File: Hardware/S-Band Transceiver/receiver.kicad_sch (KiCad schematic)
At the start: 61 parts, among them J1 SMA, J6 SMA, J8 SMA, U1 LT1819, U15 TSS-53LNB3+, U17 SKY16603-632LF, U18 LT1819, U20 DCW-22-332+, U21 ADL5906

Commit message: Updates to schematic
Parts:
- added R59: 0, symbol Device:R_Small_US
- added U4: SN74LVC1G125DCK, Package_TO_SOT_SMD:SOT-23-5, symbol 74xGxx:SN74LVC1G125DCK
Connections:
- net GND: now also R59.1, U4.3 (GND)
- net IQ_MIXER_EN: now also R59.2
- net RX_AMP_EN: now also U4.2; no longer R16.2, U15.11 (EN)
- net +3V3_RX_AMP renamed +3.3VA
- net +3.3VA: now also U4.5 (VCC)
- new net: R16.2, U15.11 (EN), U4.4

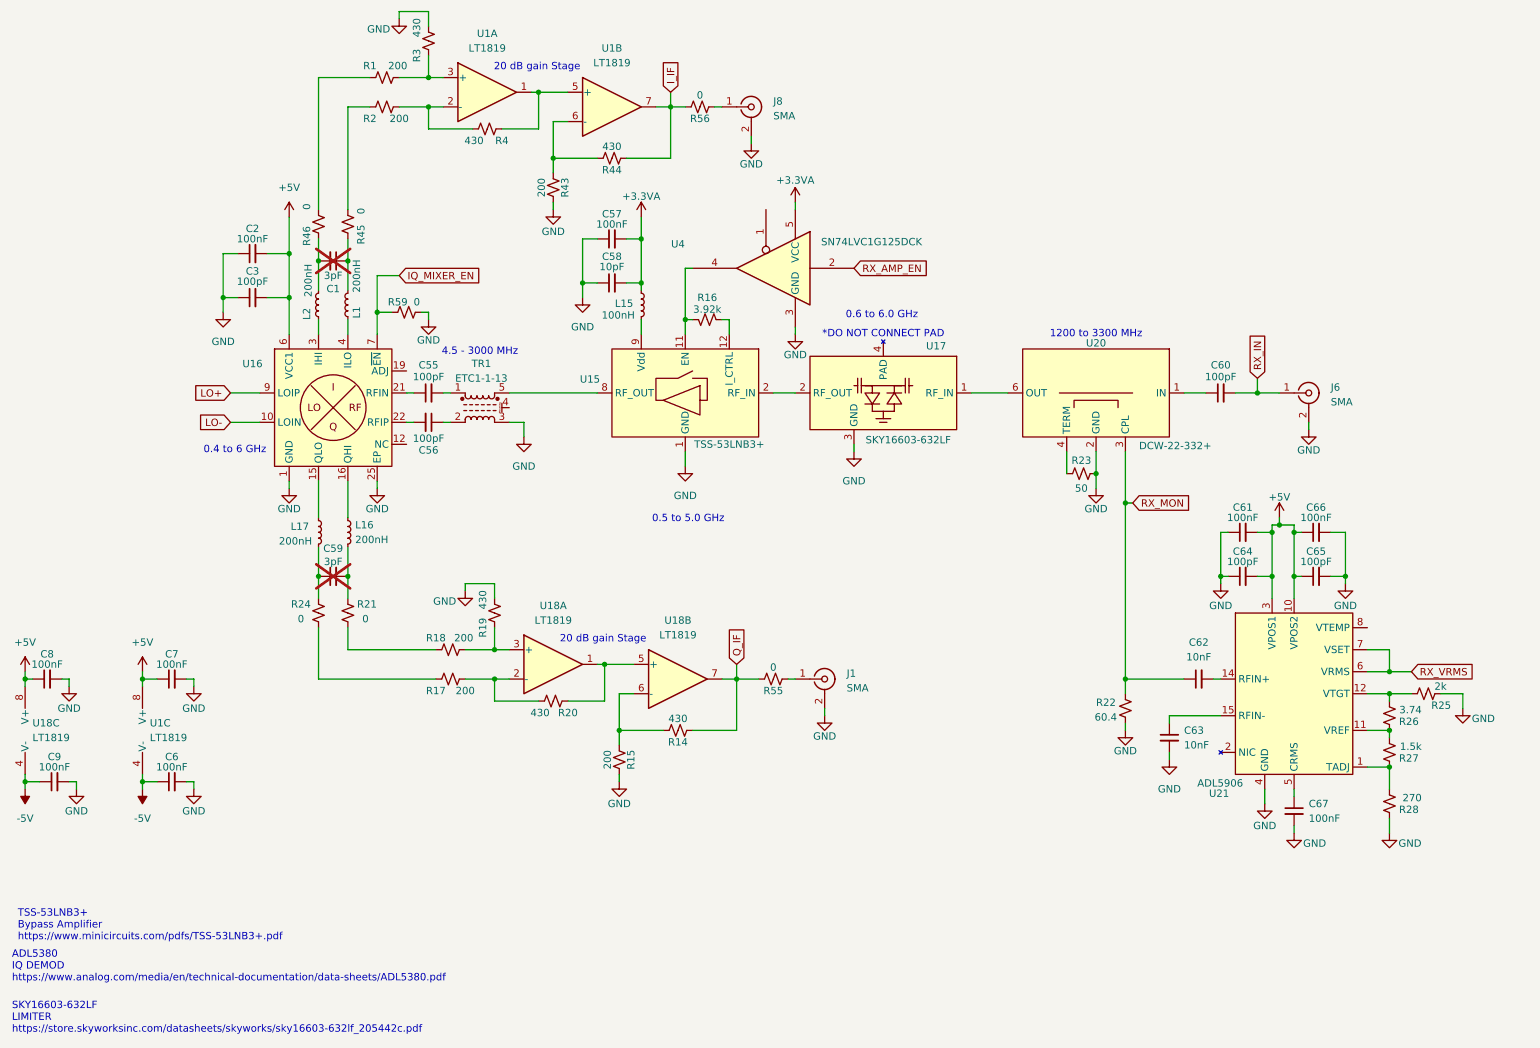
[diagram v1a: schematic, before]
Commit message: Updates to Schematic
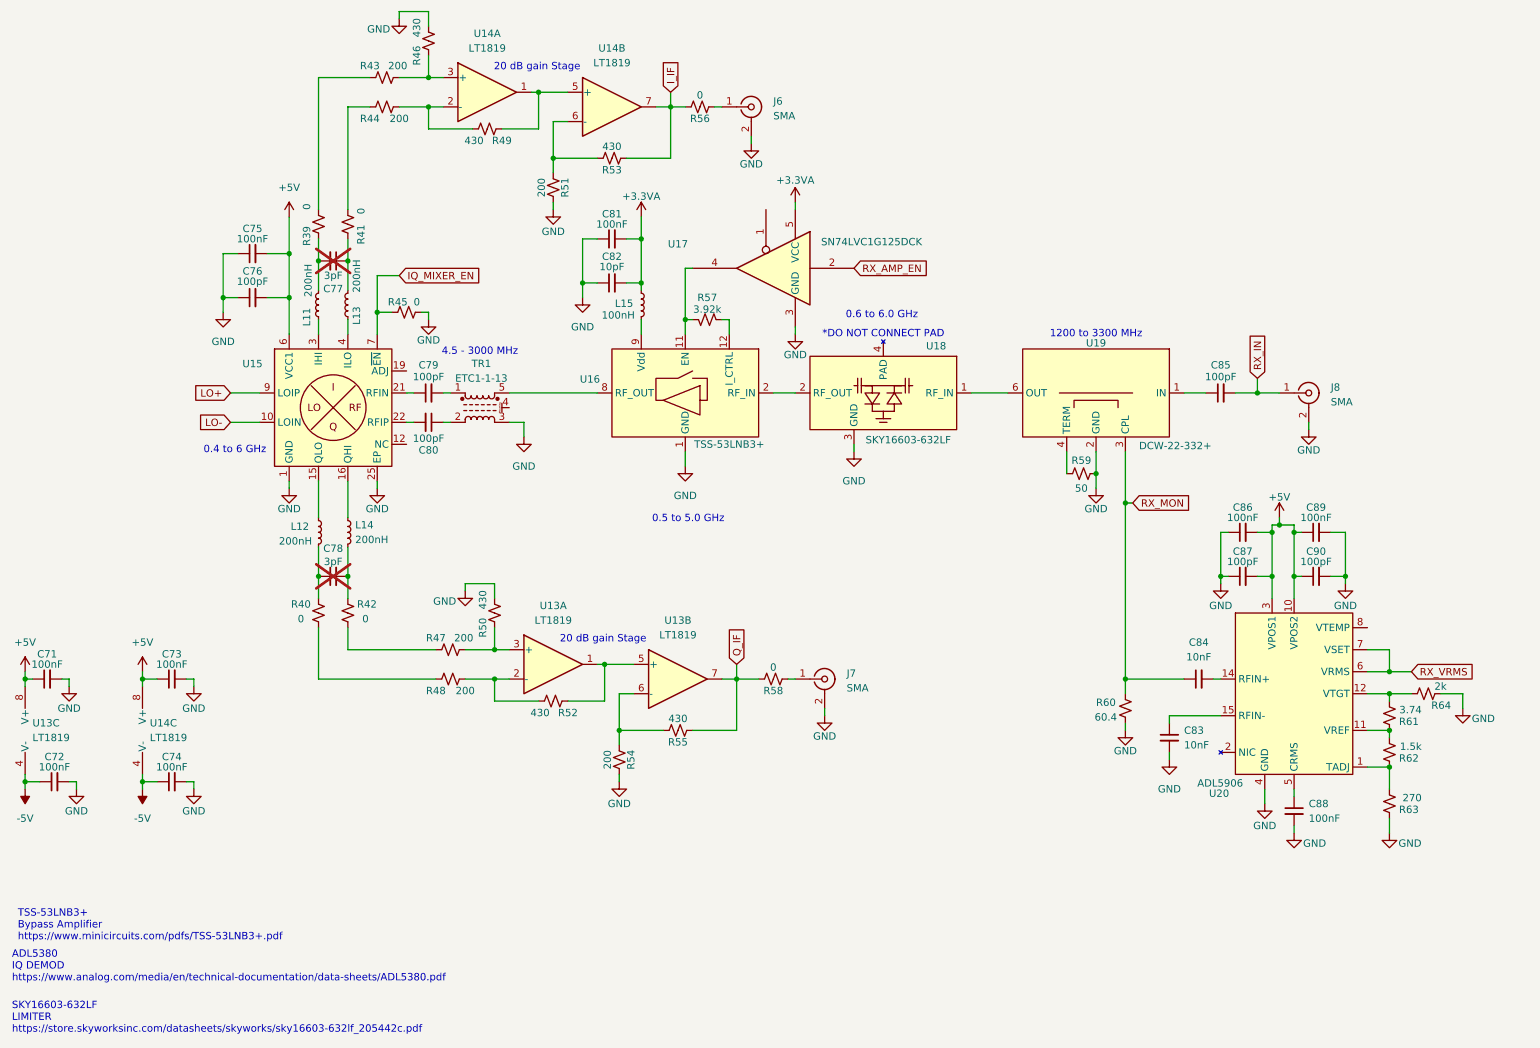
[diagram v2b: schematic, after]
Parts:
- renumbered C8 to C71, C9 to C72, C7 to C73, C6 to C74, C2 to C75, C3 to C76, C1 to C77, C59 to C78, C55 to C79, C56 to C80, C57 to C81, C58 to C82, C63 to C83, C62 to C84, C60 to C85, C61 to C86, C64 to C87, C67 to C88, C66 to C89, C65 to C90, J8 to J6, J1 to J7, J6 to J8, L2 to L11, L17 to L12, L1 to L13, L16 to L14, R46 to R39, R24 to R40, R45 to R41, R21 to R42, R1 to R43, R2 to R44, R59 to R45, R3 to R46, R18 to R47, R17 to R48, R4 to R49, R19 to R50, R43 to R51, R20 to R52, R44 to R53, R15 to R54, R14 to R55, R16 to R57, R55 to R58, R23 to R59, R22 to R60, R26 to R61, R27 to R62, R28 to R63, R25 to R64, U18 to U13, U1 to U14, U16 to U15, U15 to U16, U4 to U17, U17 to U18, U20 to U19, U21 to U20

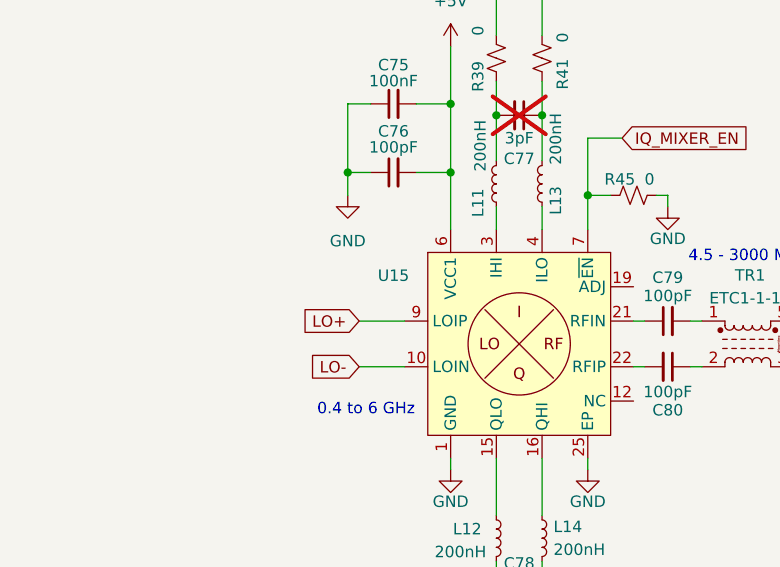
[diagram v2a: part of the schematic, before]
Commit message: Finished assigning footprints and starting board layout
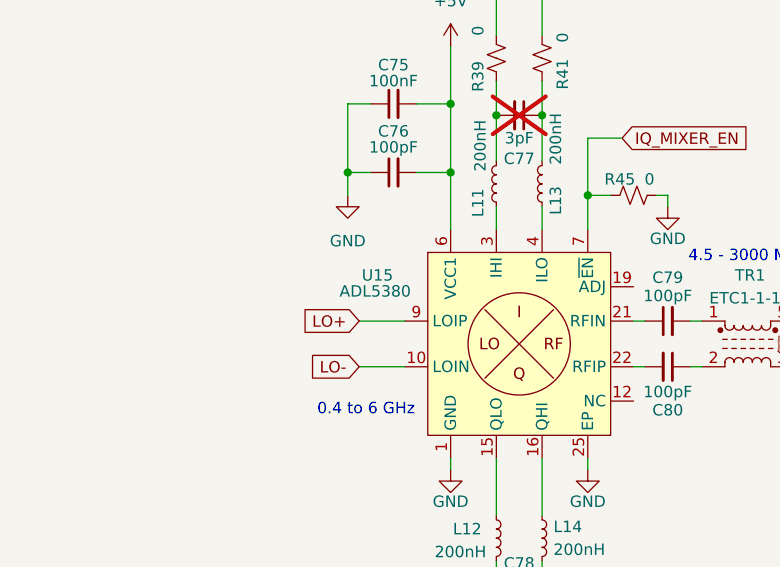
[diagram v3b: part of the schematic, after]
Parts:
- C71, C72, C73, C74, C75, C76, C77, C78, C79, C80, C81, C82, C83, C84, C85, C86, C87, C88, C89, C90: footprint (none) -> Capacitor_SMD:C_0402_1005Metric
- J6, J7, J8: footprint (none) -> Connector_Coaxial:SMA_Samtec_SMA-J-P-X-ST-EM1_EdgeMount
- L11, L12, L13, L14, L15: footprint (none) -> Inductor_SMD:L_0402_1005Metric
- R39, R40, R41, R42, R43, R44, R45, R46, R47, R48, R49, R50, R51, R52, R53, R54, R55, R56, R57, R58, R59, R60, R61, R62, R63, R64: footprint (none) -> Resistor_SMD:R_0603_1608Metric
- U15: value ~ -> ADL5380
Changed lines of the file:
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@@
 			)
 		)
-		(property "Footprint" ""
+		(property "Footprint" "Resistor_SMD:R_0603_1608Metric"
 			(at 149.86 132.08 0)
 			(effects
@@
 			)
 		)
-		(property "Footprint" ""
+		(property "Footprint" "Resistor_SMD:R_0603_1608Metric"
 			(at 133.35 140.97 0)
 			(effects
@@
 			)
 		)
-		(property "Footprint" ""
+		(property "Footprint" "Resistor_SMD:R_0603_1608Metric"
 			(at 101.6 120.65 0)
 			(effects
@@
 			)
 		)
-		(property "Footprint" ""
+		(property "Footprint" "Inductor_SMD:L_0402_1005Metric"
 			(at 127 67.31 0)
 			(effects
@@
 			)
 		)
-		(property "Footprint" ""
+		(property "Footprint" "Capacitor_SMD:C_0402_1005Metric"
 			(at 24.13 132.08 0)
 			(effects
@@
 			)
 		)
-		(property "Footprint" ""
+		(property "Footprint" "Resistor_SMD:R_0603_1608Metric"
 			(at 82.55 33.02 0)
 			(effects
@@
 			)
 		)
-		(property "Footprint" ""
+		(property "Footprint" "Capacitor_SMD:C_0402_1005Metric"
 			(at 227.33 82.55 0)
 			(effects
@@
 			)
 		)
-		(property "Footprint" ""
+		(property "Footprint" "Capacitor_SMD:C_0402_1005Metric"
 			(at 73.66 114.3 0)
 			(effects
@@
 			)
 		)
-		(property "Footprint" ""
+		(property "Footprint" "Connector_Coaxial:SMA_Samtec_SMA-J-P-X-ST-EM1_EdgeMount"
 			(at 158.75 132.08 0)
 			(effects
@@
 			)
 		)
-		(property "Footprint" ""
+		(property "Footprint" "Inductor_SMD:L_0402_1005Metric"
 			(at 71.12 67.31 0)
 			(effects
@@
 			)
 		)
-		(property "Footprint" ""
+		(property "Footprint" "Resistor_SMD:R_0603_1608Metric"
 			(at 262.89 134.62 0)
 			(effects
@@
 			)
 		)
-		(property "Footprint" ""
+		(property "Footprint" "Capacitor_SMD:C_0402_1005Metric"
 			(at 243.84 106.68 0)
 			(effects
@@
 			)
 		)
-		(property "Footprint" ""
+		(property "Footprint" "Resistor_SMD:R_0603_1608Metric"
 			(at 111.76 46.99 0)
 			(effects
@@
 			)
 		)
-		(property "Footprint" ""
+		(property "Footprint" "Resistor_SMD:R_0603_1608Metric"
 			(at 93.98 127 0)
 			(effects
@@
 			)
 		)
-		(property "Footprint" ""
+		(property "Footprint" "Resistor_SMD:R_0603_1608Metric"
 			(at 90.17 21.59 0)
 			(effects
@@
 			)
 		)
-		(property "Footprint" ""
+		(property "Footprint" "Capacitor_SMD:C_0402_1005Metric"
 			(at 121.92 63.5 0)
 			(effects
@@
 			)
 		)
-		(property "Footprint" ""
+		(property "Footprint" "Capacitor_SMD:C_0402_1005Metric"
 			(at 231.14 106.68 0)
 			(effects
@@
 			)
 		)
-		(property "Footprint" ""
+		(property "Footprint" "Resistor_SMD:R_0603_1608Metric"
 			(at 138.43 69.85 0)
 			(effects
@@
 			)
 		)
-		(property "Footprint" ""
+		(property "Footprint" "Inductor_SMD:L_0402_1005Metric"
 			(at 71.12 106.68 0)
 			(effects
@@
 			)
 		)
-		(property "Footprint" ""
+		(property "Footprint" "Connector_Coaxial:SMA_Samtec_SMA-J-P-X-ST-EM1_EdgeMount"
 			(at 242.57 82.55 0)
 			(effects
@@
 			)
 		)
-		(property "Footprint" ""
+		(property "Footprint" "Resistor_SMD:R_0603_1608Metric"
 			(at 93.98 132.08 0)
 			(effects
@@
 			)
 		)
-		(property "Footprint" ""
+		(property "Footprint" "Resistor_SMD:R_0603_1608Metric"
 			(at 137.16 33.02 0)
 			(effects
@@
 			)
 		)
-		(property "Footprint" ""
+		(property "Footprint" "Resistor_SMD:R_0603_1608Metric"
 			(at 256.54 153.67 0)
 			(effects
@@
 			)
 		)
-		(property "Footprint" ""
+		(property "Footprint" "Capacitor_SMD:C_0402_1005Metric"
 			(at 25.4 149.86 0)
 			(effects
@@
 			)
 		)
-		(property "Footprint" ""
+		(property "Footprint" "Resistor_SMD:R_0603_1608Metric"
 			(at 71.12 53.34 0)
 			(effects
@@
 			)
 		)
-		(property "Footprint" ""
+		(property "Footprint" "Capacitor_SMD:C_0402_1005Metric"
 			(at 223.52 132.08 0)
 			(effects
@@
 			)
 		)
-		(property "Footprint" ""
+		(property "Footprint" "Resistor_SMD:R_0603_1608Metric"
 			(at 210.82 137.16 0)
 			(effects
@@
 			)
 		)
-		(property "Footprint" ""
+		(property "Footprint" "Resistor_SMD:R_0603_1608Metric"
 			(at 123.19 146.05 0)
 			(effects
@@
 		(on_board yes)
 		(dnp no)
-		(fields_autoplaced yes)
 		(property "Reference" "U15"
-			(at 59.69 77.5014 0)
+			(at 57.912 77.47 0)
 			(effects
 				(font
@@
 			)
 		)
-		(property "Value" "~"
-			(at 59.69 79.4065 0)
+		(property "Value" "ADL5380"
+			(at 57.658 79.248 0)
 			(effects
 				(font
@@
 			)
 		)
-		(property "Footprint" ""
+		(property "Footprint" "Inductor_SMD:L_0402_1005Metric"
 			(at 76.2 67.31 0)
 			(effects
@@
 			)
 		)
-		(property "Footprint" ""
+		(property "Footprint" "Connector_Coaxial:SMA_Samtec_SMA-J-P-X-ST-EM1_EdgeMount"
 			(at 146.05 33.02 0)
 			(effects
@@
 			)
 		)
-		(property "Footprint" ""
+		(property "Footprint" "Resistor_SMD:R_0603_1608Metric"
 			(at 86.36 68.58 0)
 			(effects
@@
 			)
 		)
-		(property "Footprint" ""
+		(property "Footprint" "Resistor_SMD:R_0603_1608Metric"
 			(at 256.54 138.43 0)
 			(effects
@@
 			)
 		)
-		(property "Footprint" ""
+		(property "Footprint" "Resistor_SMD:R_0603_1608Metric"
 			(at 203.2 96.52 0)
 			(effects
@@
 			)
 		)
-		(property "Footprint" ""
+		(property "Footprint" "Inductor_SMD:L_0402_1005Metric"
 			(at 76.2 106.68 0)
 			(effects
@@
 			)
 		)
-		(property "Footprint" ""
+		(property "Footprint" "Resistor_SMD:R_0603_1608Metric"
 			(at 82.55 27.94 0)
 			(effects
@@
 			)
 		)
-		(property "Footprint" ""
+		(property "Footprint" "Capacitor_SMD:C_0402_1005Metric"
 			(at 218.44 142.24 0)
 			(effects
@@
 			)
 		)
-		(property "Footprint" ""
+		(property "Footprint" "Capacitor_SMD:C_0402_1005Metric"
 			(at 90.17 82.55 0)
 			(effects
@@
 			)
 		)
-		(property "Footprint" ""
+		(property "Footprint" "Capacitor_SMD:C_0402_1005Metric"
 			(at 90.17 87.63 0)
 			(effects
@@
 			)
 		)
-		(property "Footprint" ""
+		(property "Footprint" "Capacitor_SMD:C_0402_1005Metric"
 			(at 73.66 59.69 0)
 			(effects
@@
 			)
 		)
-		(property "Footprint" ""
+		(property "Footprint" "Capacitor_SMD:C_0402_1005Metric"
 			(at 121.92 55.88 0)
 			(effects
@@
 			)
 		)
-		(property "Footprint" ""
+		(property "Footprint" "Capacitor_SMD:C_0402_1005Metric"
 			(at 45.72 149.86 0)
 			(effects
@@
 			)
 		)
-		(property "Footprint" ""
+		(property "Footprint" "Capacitor_SMD:C_0402_1005Metric"
 			(at 240.03 154.94 0)
 			(effects
@@
 			)
 		)
-		(property "Footprint" ""
+		(property "Footprint" "Resistor_SMD:R_0603_1608Metric"
 			(at 76.2 53.34 0)
 			(effects
@@
 			)
 		)
-		(property "Footprint" ""
+		(property "Footprint" "Resistor_SMD:R_0603_1608Metric"
 			(at 100.33 36.83 0)
 			(effects
@@
 			)
 		)
-		(property "Footprint" ""
+		(property "Footprint" "Resistor_SMD:R_0603_1608Metric"
 			(at 111.76 135.89 0)
 			(effects
@@
 			)
 		)
-		(property "Footprint" ""
+		(property "Footprint" "Capacitor_SMD:C_0402_1005Metric"
 			(at 45.72 132.08 0)
 			(effects
@@
 			)
 		)
-		(property "Footprint" ""
+		(property "Footprint" "Capacitor_SMD:C_0402_1005Metric"
 			(at 59.69 66.04 0)
 			(effects
@@
 			)
 		)
-		(property "Footprint" ""
+		(property "Footprint" "Resistor_SMD:R_0603_1608Metric"
 			(at 121.92 41.91 0)
 			(effects
@@
 			)
 		)
-		(property "Footprint" ""
+		(property "Footprint" "Capacitor_SMD:C_0402_1005Metric"
 			(at 231.14 114.3 0)
 			(effects
@@
 			)
 		)
-		(property "Footprint" ""
+		(property "Footprint" "Capacitor_SMD:C_0402_1005Metric"
 			(at 243.84 114.3 0)
 			(effects
@@
 			)
 		)
-		(property "Footprint" ""
+		(property "Footprint" "Resistor_SMD:R_0603_1608Metric"
 			(at 71.12 120.65 0)
 			(effects
@@
 			)
 		)
-		(property "Footprint" ""
+		(property "Footprint" "Resistor_SMD:R_0603_1608Metric"
 			(at 256.54 144.78 0)
 			(effects
@@
 			)
 		)
-		(property "Footprint" ""
+		(property "Footprint" "Capacitor_SMD:C_0402_1005Metric"
 			(at 59.69 58.42 0)
 			(effects
@@
 			)
 		)
-		(property "Footprint" ""
+		(property "Footprint" "Resistor_SMD:R_0603_1608Metric"
 			(at 76.2 120.65 0)
 			(effects
